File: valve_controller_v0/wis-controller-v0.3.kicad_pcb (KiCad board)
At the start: 2 copper layers, 78 x 110 mm, 68 parts, among them J1 18650 Socket, J11 Solenoid_connector, J3 USB_C_Receptacle_USB2.0, J5 SWD, J6 JST-2PH, Q1 DMG3415UQ-7, SW1 RESET, SW3 SW_DIP_x02, SW4 BOOT, U1 RAK3172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

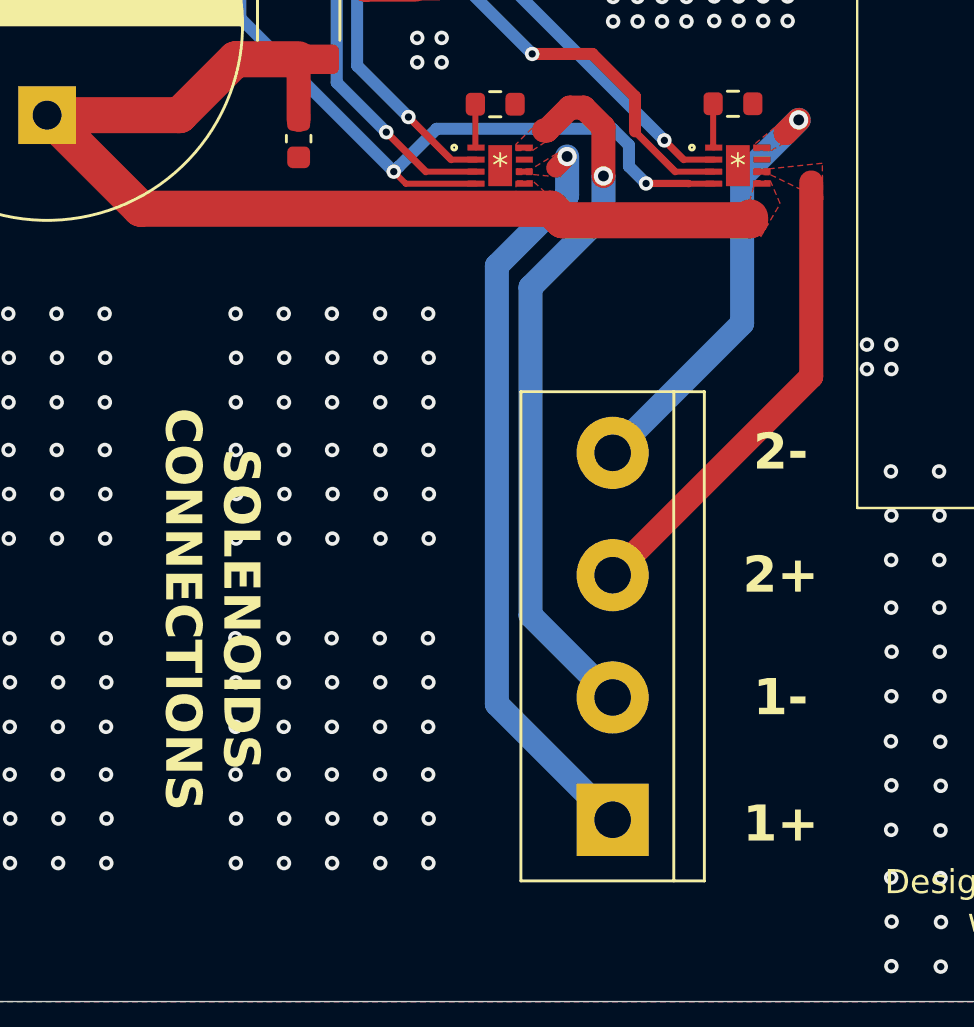
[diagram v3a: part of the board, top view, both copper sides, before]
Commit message: Corected the location of the solenoid connector
Reverted the modification of the solenoid connector to maintain its original position
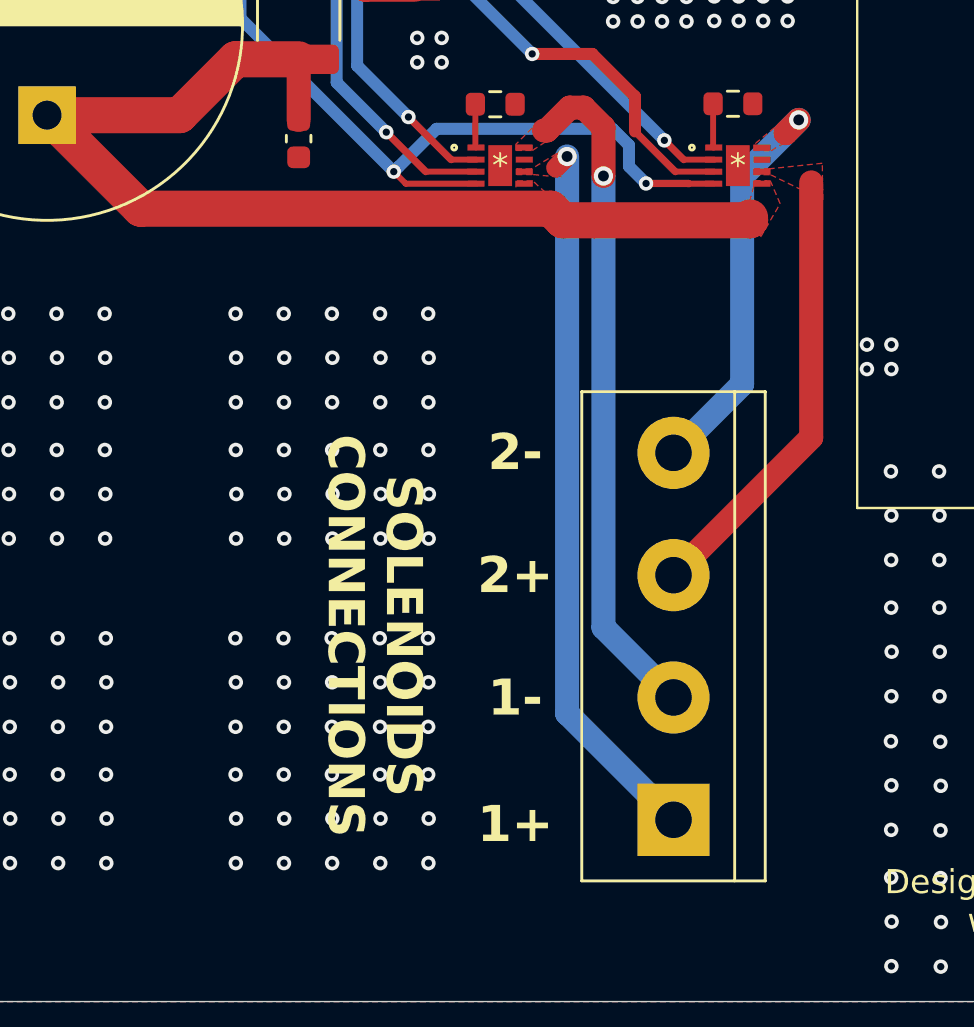
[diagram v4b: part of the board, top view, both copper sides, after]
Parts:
- moved J11 2.53 mm to (146.0, 122.5)
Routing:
- net Net-(J11-Pin_2): track 29.6 -> 28.1 mm
- net Net-(J11-Pin_1): track 31.4 -> 30.0 mm
- net Net-(J11-Pin_3): track 19.7 -> 18.7 mm
- net Net-(J11-Pin_4): track 17.9 -> 16.8 mm
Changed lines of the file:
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@@
 	(footprint "TerminalBlock:TerminalBlock_bornier-4_P5.08mm"
 		(layer "F.Cu")
-		(at 143.491463 122.45 90)
+		(at 146.02 122.45 90)
 		(descr "simple 4-pin terminal block, pitch 5.08mm, revamped version of bornier4")
 		(tags "terminal block bornier4")
@@
 	)
 	(gr_text "2-"
-		(at 150.471463 107.17 0)
+		(at 139.446 107.188 0)
 		(layer "F.SilkS")
 		(effects
@@
 	)
 	(gr_text "2+"
-		(at 150.471463 112.28 0)
+		(at 139.446 112.298 0)
 		(layer "F.SilkS")
 		(effects
@@
 	)
 	(gr_text "1-"
-		(at 150.471463 117.37 0)
+		(at 139.446 117.388 0)
 		(layer "F.SilkS")
 		(effects
@@
 	)
 	(gr_text "1+"
-		(at 150.471463 122.62 0)
+		(at 139.446 122.638 0)
 		(layer "F.SilkS")
 		(effects
@@
 	)
 	(gr_text "SOLENOIDS\nCONNECTIONS"
-		(at 126.85 113.71 270)
+		(at 133.604 114.808 270)
 		(layer "F.SilkS")
 		(effects
@@
 	)
 	(segment
-		(start 138.684 99.441)
-		(end 138.684 117.642537)
-		(width 1)
-		(layer "B.Cu")
-		(net 44)
-	)
-	(segment
-		(start 141.6 96.525)
-		(end 138.684 99.441)
-		(width 1)
-		(layer "B.Cu")
-		(net 44)
-	)
-	(segment
 		(start 141.6 94.9)
-		(end 141.6 96.525)
+		(end 141.6 118.03)
 		(width 1)
 		(layer "B.Cu")
@@
 	)
 	(segment
-		(start 138.684 117.642537)
-		(end 143.491463 122.45)
+		(start 141.6 118.03)
+		(end 146.02 122.45)
 		(width 1)
 		(layer "B.Cu")
@@
 	)
 	(segment
-		(start 140.081 113.959537)
-		(end 143.491463 117.37)
-		(width 1)
-		(layer "B.Cu")
-		(net 45)
-	)
-	(segment
 		(start 143.11 95.71)
-		(end 143.11 97.301)
-		(width 1)
-		(layer "B.Cu")
-		(net 45)
-	)
-	(segment
-		(start 140.081 100.33)
-		(end 140.081 113.959537)
+		(end 143.11 114.46)
 		(width 1)
 		(layer "B.Cu")
@@
 	)
 	(segment
-		(start 143.11 97.301)
-		(end 140.081 100.33)
+		(start 143.11 114.46)
+		(end 146.02 117.37)
 		(width 1)
 		(layer "B.Cu")
@@
 	)
 	(segment
-		(start 143.491463 112.29)
-		(end 151.74 104.041463)
+		(start 146.02 112.29)
+		(end 151.74 106.57)
 		(width 1)
 		(layer "F.Cu")
@@
 	)
 	(segment
-		(start 151.74 104.041463)
+		(start 151.74 106.57)
 		(end 151.74 95.977164)
 		(width 1)
@@
 	)
 	(segment
-		(start 148.87 95.73)
-		(end 148.87 101.831463)
+		(start 148.87 104.36)
+		(end 146.02 107.21)
 		(width 1)
 		(layer "B.Cu")
@@
 	)
 	(segment
-		(start 151.22 93.38)
-		(end 148.87 95.73)
+		(start 148.87 95.73)
+		(end 148.87 104.36)
 		(width 1)
 		(layer "B.Cu")
@@
 	)
 	(segment
-		(start 148.87 101.831463)
-		(end 143.491463 107.21)
+		(start 151.22 93.38)
+		(end 148.87 95.73)
 		(width 1)
 		(layer "B.Cu")
